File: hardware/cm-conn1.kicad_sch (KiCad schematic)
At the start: 7 parts, among them J3 RJ45_RB1-125B8G1A

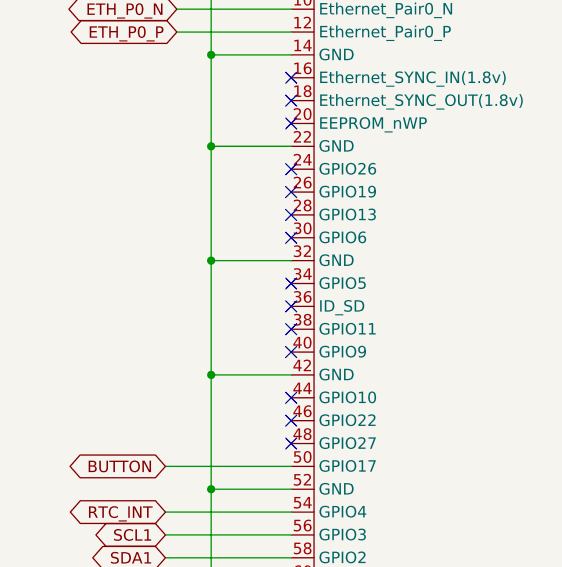
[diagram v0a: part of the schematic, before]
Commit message: FDS4435BZ: hide pin numbers, fix footprint refs, add SATA_PWR_EN label
- Clean up FDS4435BZ symbol (hidden pin numbers)
- Fix Pedalboard Library → granit footprint references
- Sync embedded symbols with library
- GPIO5 labeled as SATA_PWR_EN for future power switching
- 1 warning: isolated SATA_PWR_EN (pending SATA FET placement)
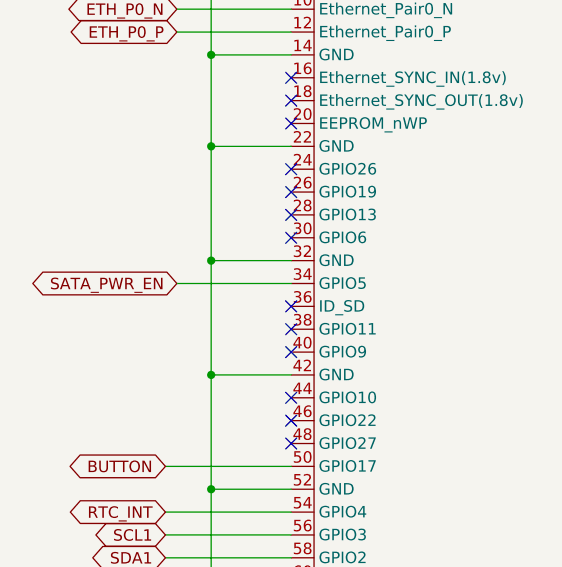
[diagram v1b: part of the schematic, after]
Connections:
- net SATA_PWR_EN: now reaches CM1.34 (GPIO5)
- no-connect marks 49 -> 48
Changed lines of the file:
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@@
-	)
-	(no_connect
-		(at 54.61 81.28)
 	)
 	(no_connect
@@
 		(pts
 			(xy 54.61 40.64) (xy 45.72 40.64)
+		)
+		(stroke
+			(width 0)
+			(type default)
+		)
+	)
+	(wire
+		(pts
+			(xy 41.91 81.28) (xy 54.61 81.28)
 		)
 		(stroke
@@
 			(hide yes)
 			(show_name no)
+			(do_not_autoplace no)
+			(effects
+				(font
+					(size 1.27 1.27)
+				)
+				(justify right)
+			)
+		)
+	)
+	(global_label "SATA_PWR_EN"
+		(shape bidirectional)
+		(at 41.91 81.28 180)
+		(fields_autoplaced yes)
+		(effects
+			(font
+				(size 1.27 1.27)
+			)
+			(justify right)
+		)
+		(property "Intersheetrefs" "${INTERSHEET_REFS}"
+			(at 25.0531 81.28 0)
+			(hide yes)
+			(show_name no)

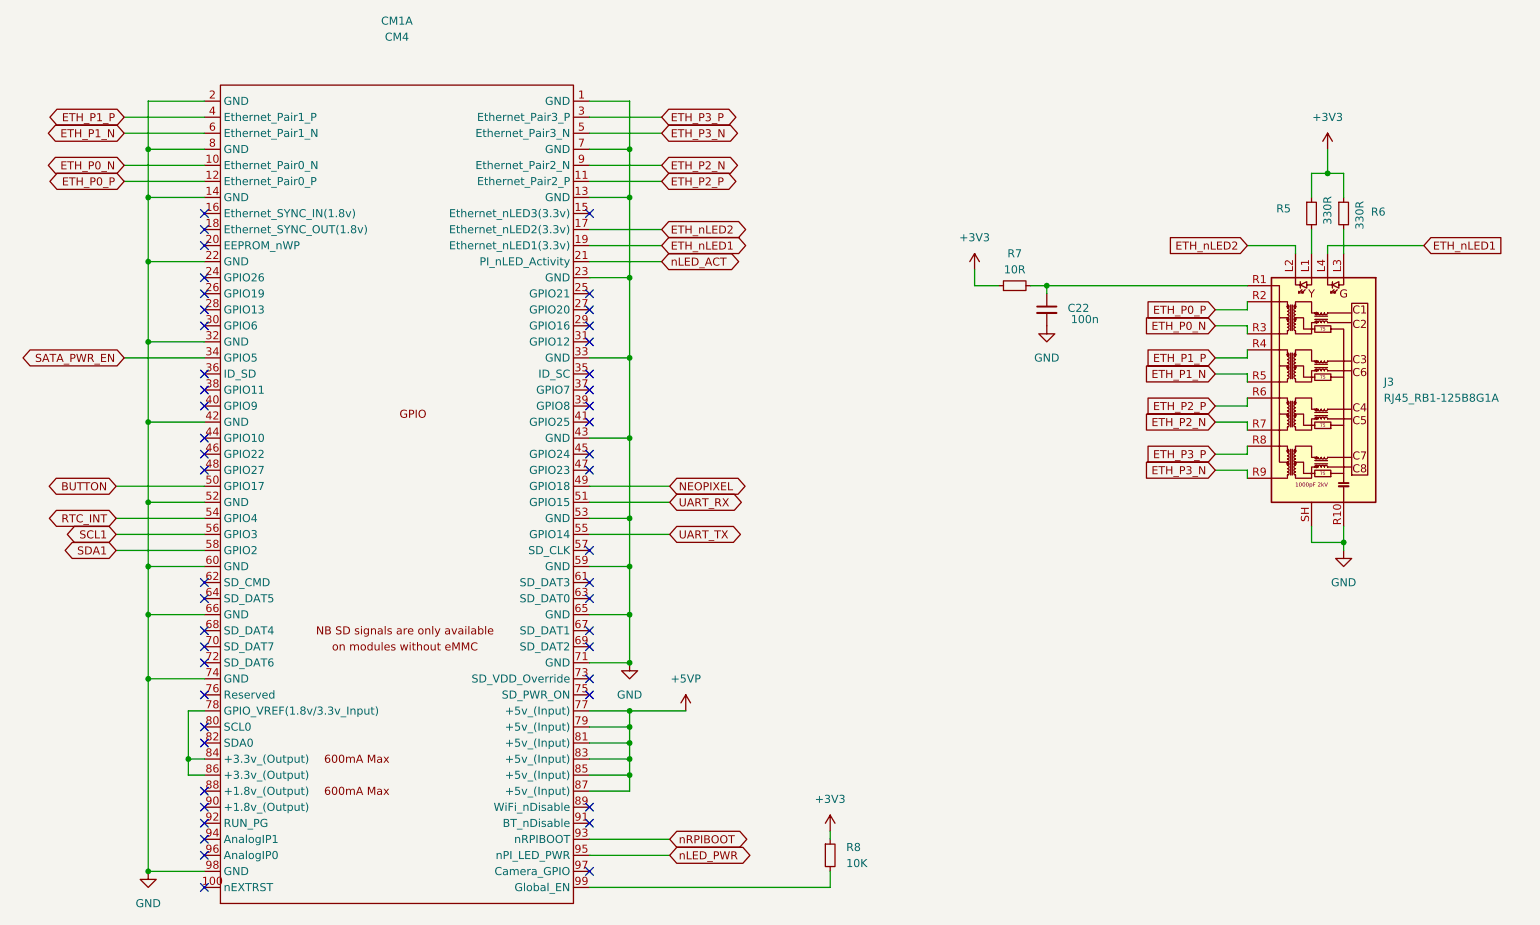
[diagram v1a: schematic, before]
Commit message: Add hardware wake circuit: 2N7002 + 74AHCT1G32 OR gate
RTC alarm → N-FET inverter → OR gate → GLOBAL_EN
GPIO6 (GPIO_HOLD) keeps CM4 alive after boot.
All wake components DNP for v1 (pull-up fallback).
v2: populate wake circuit, remove GLOBAL_EN pull-up.
ERC: 0 errors, 0 warnings
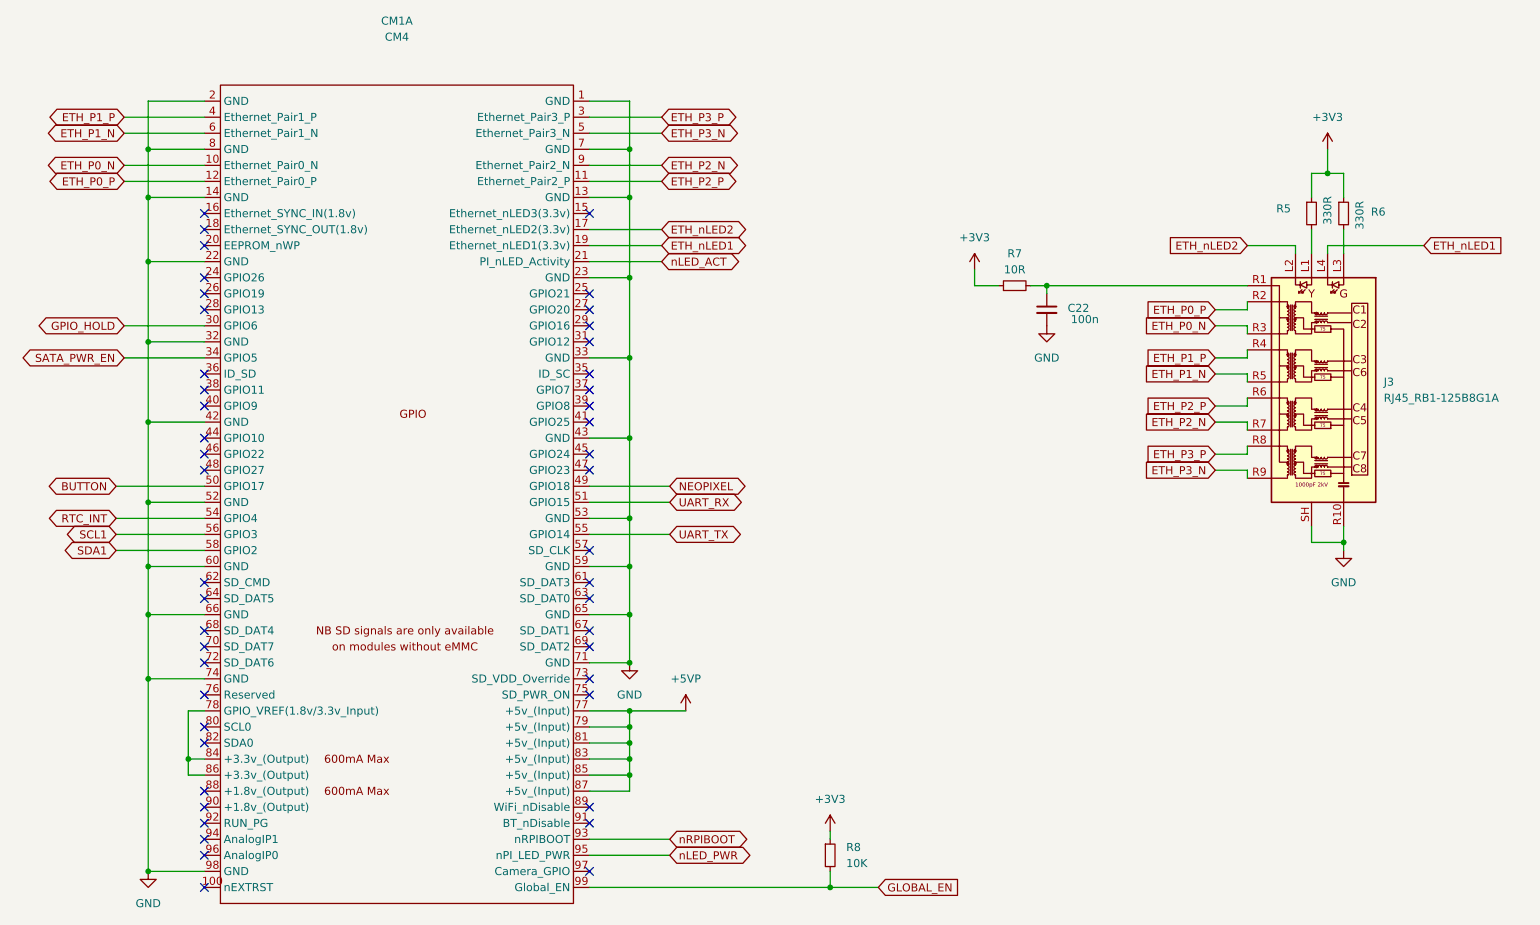
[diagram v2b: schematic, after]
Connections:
- net GPIO_HOLD: now reaches CM1.30 (GPIO6)
- net GLOBAL_EN: now reaches CM1.99 (Global_EN), R8.2
- no-connect marks 48 -> 47
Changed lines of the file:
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@@
+	)
+	(junction
+		(at 153.67 165.1)
+		(diameter 0)
+		(color 0 0 0 0)
 	)
 	(junction
@@
 	)
 	(no_connect
-		(at 54.61 76.2)
-	)
-	(no_connect
 		(at 115.57 162.56)
 	)
@@
 	(wire
 		(pts
+			(xy 115.57 165.1) (xy 153.67 165.1)
+		)
+		(stroke
+			(width 0)
+			(type default)
+		)
+	)
+	(wire
+		(pts
 			(xy 229.87 110.49) (xy 234.95 110.49)
 		)
@@
 	(wire
 		(pts
+			(xy 41.91 76.2) (xy 54.61 76.2)
+		)
+		(stroke
+			(width 0)
+			(type default)
+		)
+	)
+	(wire
+		(pts
 			(xy 214.63 91.44) (xy 219.71 91.44)
 		)
@@
 	(wire
 		(pts
+			(xy 153.67 165.1) (xy 161.29 165.1)
+		)
+		(stroke
+			(width 0)
+			(type default)
+		)
+	)
+	(wire
+		(pts
 			(xy 115.57 40.64) (xy 121.92 40.64)
 		)
@@
 		(pts
 			(xy 115.57 104.14) (xy 128.27 104.14)
-		)
-		(stroke
-			(width 0)
-			(type default)
-		)
-	)
-	(wire
-		(pts
-			(xy 115.57 165.1) (xy 153.67 165.1)
 		)
 		(stroke
@@
 		)
 	)
-	(global_label "ETH_P3_P"
-		(shape input)
-		(at 214.63 96.52 180)
+	(global_label "GPIO_HOLD"
+		(shape bidirectional)
+		(at 41.91 76.2 180)
 		(fields_autoplaced yes)
 		(effects
@@
 		)
 		(property "Intersheetrefs" "${INTERSHEET_REFS}"
-			(at 202.513 96.52 0)
+			(at 27.4115 76.2 0)
 			(hide yes)
 			(show_name no)
@@
 		)
 	)
-	(global_label "ETH_P1_P"
-		(shape bidirectional)
-		(at 41.91 43.18 180)
+	(global_label "ETH_P3_P"
+		(shape input)
+		(at 214.63 96.52 180)
 		(fields_autoplaced yes)
 		(effects
@@
 		)
 		(property "Intersheetrefs" "${INTERSHEET_REFS}"
-			(at 28.6817 43.18 0)
+			(at 202.513 96.52 0)
 			(hide yes)
 			(show_name no)
@@
 		)
 	)
-	(global_label "BUTTON"
+	(global_label "ETH_P1_P"
 		(shape bidirectional)
-		(at 40.64 101.6 180)
+		(at 41.91 43.18 180)
 		(fields_autoplaced yes)
 		(effects
@@
 		)
 		(property "Intersheetrefs" "${INTERSHEET_REFS}"
-			(at 29.3468 101.6 0)
+			(at 28.6817 43.18 0)
 			(hide yes)
 			(show_name no)
@@
 		)
 	)
+	(global_label "BUTTON"
+		(shape bidirectional)
+		(at 40.64 101.6 180)
+		(fields_autoplaced yes)
+		(effects
+			(font
+				(size 1.27 1.27)
+			)
+			(justify right)
+		)
+		(property "Intersheetrefs" "${INTERSHEET_REFS}"
+			(at 29.3468 101.6 0)
+			(hide yes)
+			(show_name no)
+			(do_not_autoplace no)
+			(effects
+				(font
+					(size 1.27 1.27)
+				)
+				(justify right)
+			)
+		)
+	)
 	(global_label "nRPIBOOT"
 		(shape bidirectional)
@@
 			(hide yes)
 			(show_name no)
+			(do_not_autoplace no)
+			(effects
+				(font
+					(size 1.27 1.27)
+				)
+				(justify left)
+			)
+		)
+	)
+	(global_label "GLOBAL_EN"
+		(shape input)
+		(at 161.29 165.1 0)
+		(fields_autoplaced yes)
+		(effects
+			(font
+				(size 1.27 1.27)
+			)
+			(justify left)
+		)
+		(property "Intersheetrefs" "${INTERSHEET_REFS}"
+			(at 174.7376 165.1 0)
+			(hide yes)
+			(show_name no)

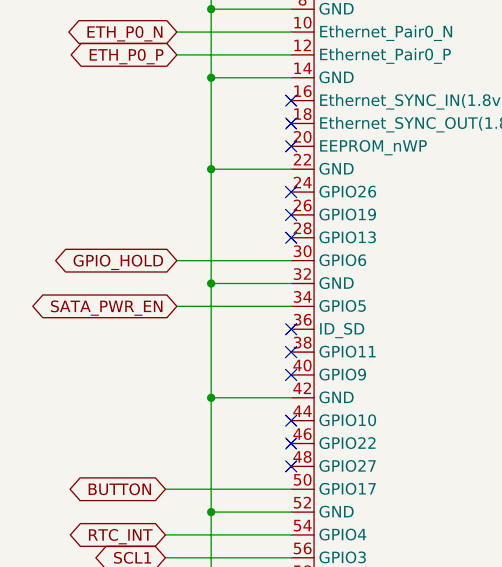
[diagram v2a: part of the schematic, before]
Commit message: Swap GPIO_HOLD and SATA_PWR_EN pin assignments for easier routing
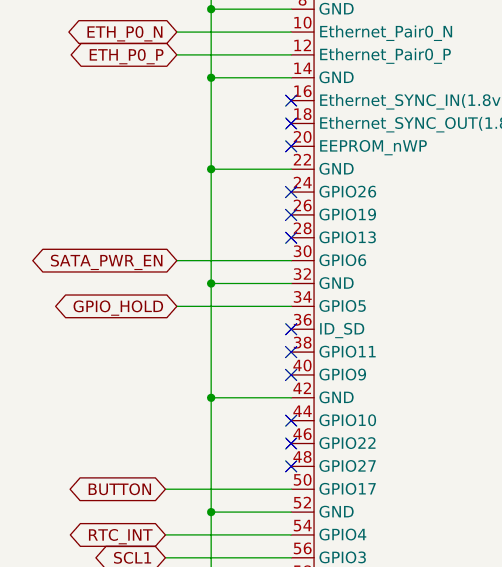
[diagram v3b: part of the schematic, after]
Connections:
- net GPIO_HOLD: now also CM1.34 (GPIO5); no longer CM1.30 (GPIO6)
- net SATA_PWR_EN: now also CM1.30 (GPIO6); no longer CM1.34 (GPIO5)
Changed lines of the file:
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@@
 		)
 	)
-	(global_label "GPIO_HOLD"
+	(global_label "SATA_PWR_EN"
 		(shape bidirectional)
 		(at 41.91 76.2 180)
@@
 		)
 		(property "Intersheetrefs" "${INTERSHEET_REFS}"
-			(at 27.4115 76.2 0)
+			(at 25.0531 76.2 0)
 			(hide yes)
 			(show_name no)
@@
 		)
 	)
-	(global_label "SATA_PWR_EN"
+	(global_label "GPIO_HOLD"
 		(shape bidirectional)
 		(at 41.91 81.28 180)
@@
 		)
 		(property "Intersheetrefs" "${INTERSHEET_REFS}"
-			(at 25.0531 81.28 0)
-			(hide yes)
-			(show_name no)
+			(at 27.4115 81.28 0)
+			(hide yes)
+			(show_name no)

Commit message: Place fiducials, continue routing
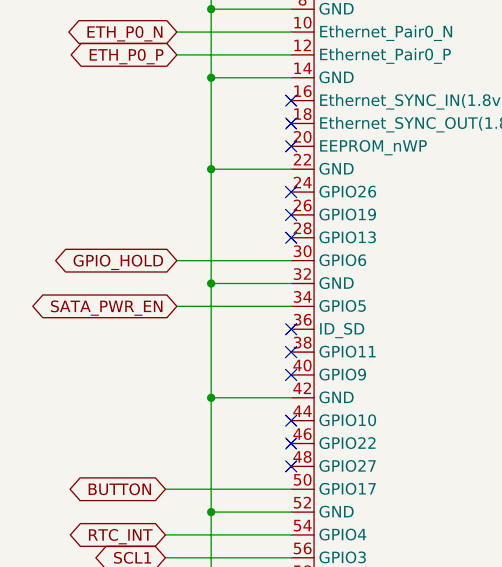
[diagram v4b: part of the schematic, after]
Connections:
- net GPIO_HOLD: now also CM1.30 (GPIO6); no longer CM1.34 (GPIO5)
- net SATA_PWR_EN: now also CM1.34 (GPIO5); no longer CM1.30 (GPIO6)
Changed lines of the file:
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@@
 		)
 	)
-	(global_label "SATA_PWR_EN"
+	(global_label "GPIO_HOLD"
 		(shape bidirectional)
 		(at 41.91 76.2 180)
@@
 		)
 		(property "Intersheetrefs" "${INTERSHEET_REFS}"
-			(at 25.0531 76.2 0)
+			(at 27.4115 76.2 0)
 			(hide yes)
 			(show_name no)
@@
 		)
 	)
-	(global_label "GPIO_HOLD"
+	(global_label "SATA_PWR_EN"
 		(shape bidirectional)
 		(at 41.91 81.28 180)
@@
 		)
 		(property "Intersheetrefs" "${INTERSHEET_REFS}"
-			(at 27.4115 81.28 0)
-			(hide yes)
-			(show_name no)
+			(at 25.0531 81.28 0)
+			(hide yes)
+			(show_name no)
